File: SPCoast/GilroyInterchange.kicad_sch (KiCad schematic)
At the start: 72 parts, among them SW5777 777, SW5781 781

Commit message: chore(kicad): owner edits: Remote-IO node fields (Kind CMRI / MQTT-JMRI, bytes, UA), Interlocking Name, IOBus pins on remote drivers, sheet cleanup
Owner's edits of 2026-10-22, committed as they stand before the read-back.
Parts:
- added Proc1: Luchessa, symbol Railroad-HardwareIO:Processor
- Plant5001: Name (none) -> ${Value}
- RIO2: Board JMRI -> (none); Kind REMOTE_IO -> MQTT-JMRI; Role STRUCTURE -> REMOTE_IO
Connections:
- net Host: now also Proc1.1 (Host)
- net IOBus: now also JMRI_MQTT1.2 (IOBus), JMRI_MQTT10.2 (IOBus), JMRI_MQTT11.2 (IOBus), JMRI_MQTT12.2 (IOBus), JMRI_MQTT13.2 (IOBus), JMRI_MQTT14.2 (IOBus), JMRI_MQTT15.2 (IOBus), JMRI_MQTT16.2 (IOBus), JMRI_MQTT2.2 (IOBus), JMRI_MQTT3.3 (IOBus), JMRI_MQTT4.3 (IOBus), JMRI_MQTT5.2 (IOBus), JMRI_MQTT6.2 (IOBus), JMRI_MQTT7.2 (IOBus), JMRI_MQTT8.2 (IOBus), JMRI_MQTT9.2 (IOBus)
- new net: GPIO5.2 (IOBus), Proc1.2 (IO_Bus)
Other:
- sheet Panel ports: added IOBus; removed I2C

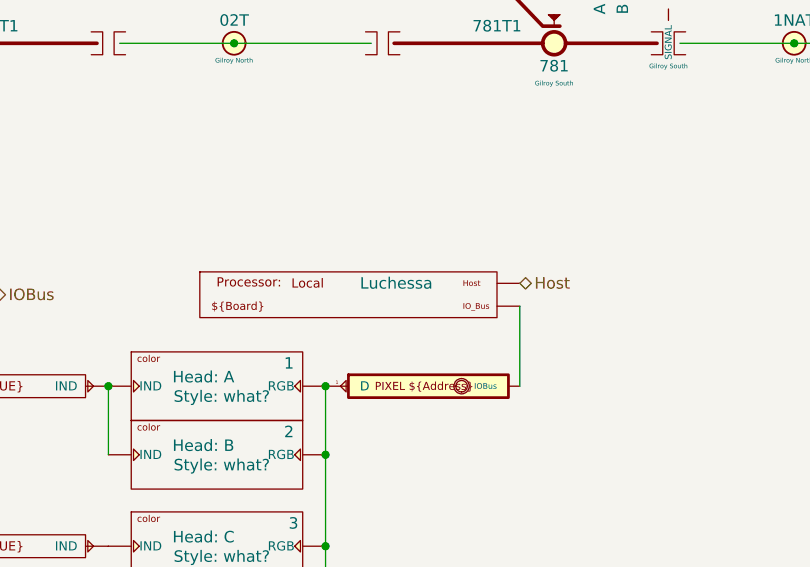
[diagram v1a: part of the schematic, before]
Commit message: chore(kicad): owner edits: JohnCTC re-landed, Interchange processor named and hosted, SPCoastApp as Processor, node Transport cleared, library defaults emptied
Owner's fixes of 2026-10-22 (items 1-5 of the read-back), committed as they stand.
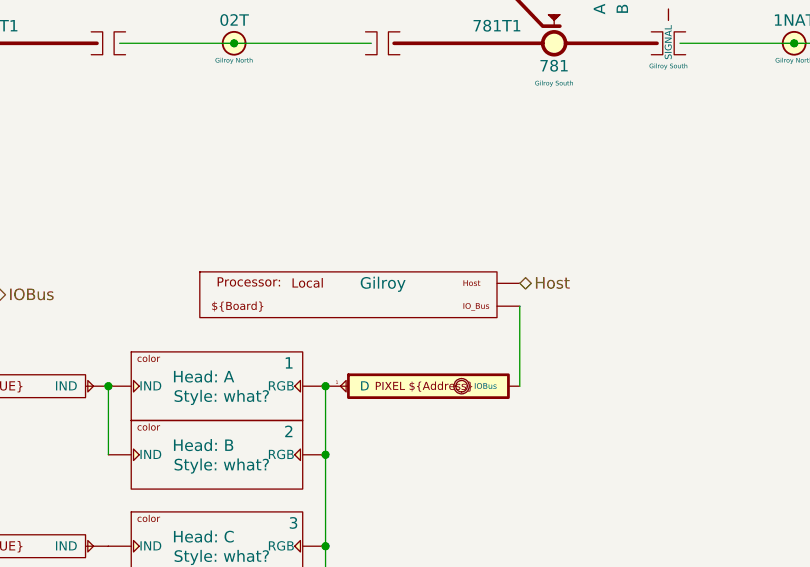
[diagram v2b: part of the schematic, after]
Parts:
- Proc1: value Luchessa -> Gilroy
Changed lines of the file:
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@@
 			)
 		)
-		(property "Value" "Luchessa"
+		(property "Value" "Gilroy"
 			(at 134.62 104.14 0)
 			(show_name no)
